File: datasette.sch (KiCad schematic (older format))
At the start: 40 parts, among them CN15 CONN_IEC_INT, CN16 CONN_TAPE_INT, CN3 CASSETTE, CN7 SERIAL_BUS, CN93 C64_STYLE_CASSETTE, Q5 2SD880, U9 74LS06, U91 DT1042, U92 DT1042

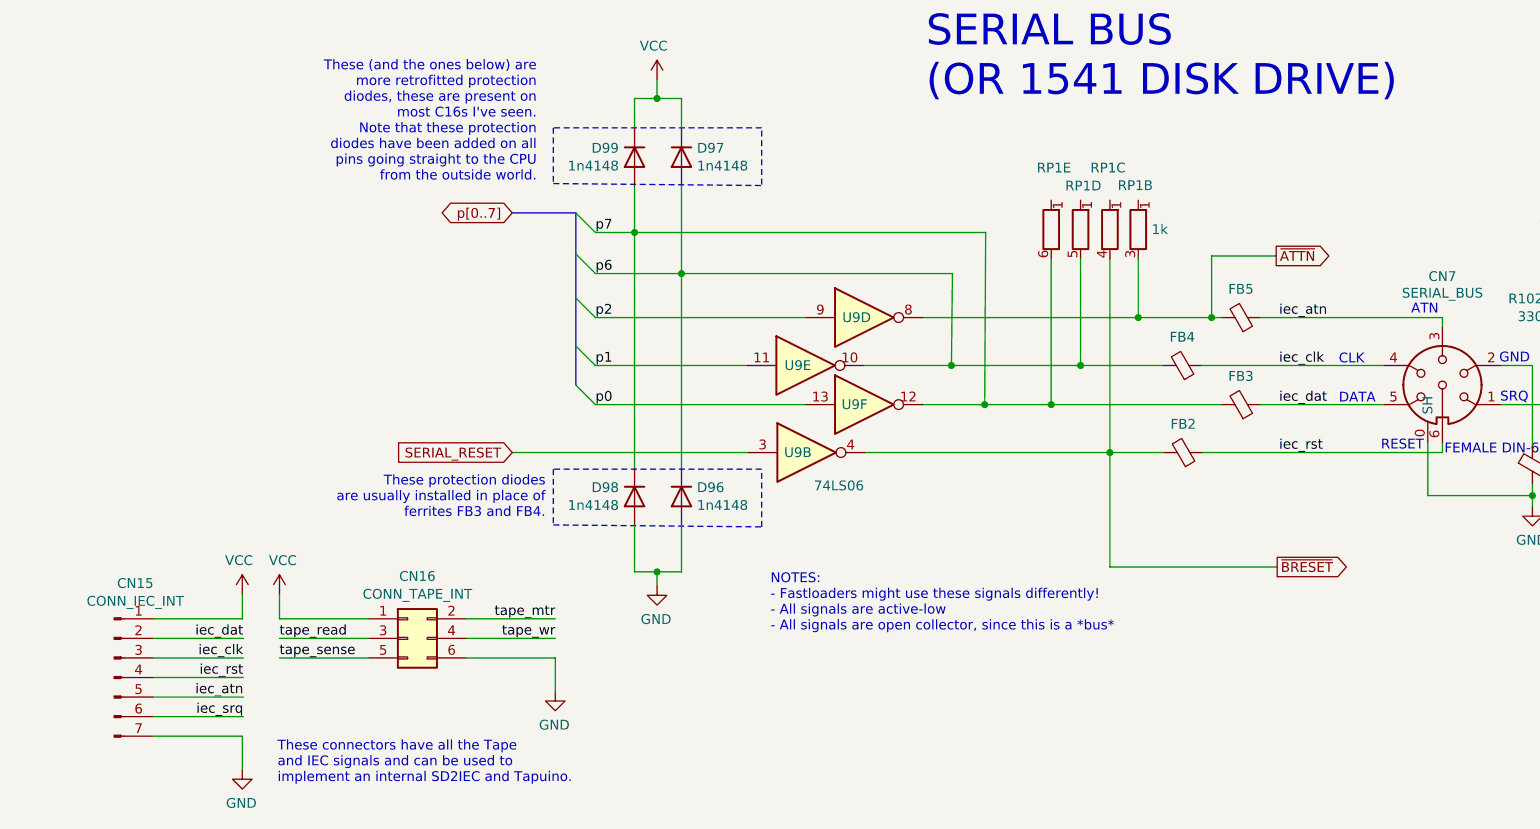
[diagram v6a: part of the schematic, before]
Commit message: Add jumper to select which reset signal is brought to IEC connector
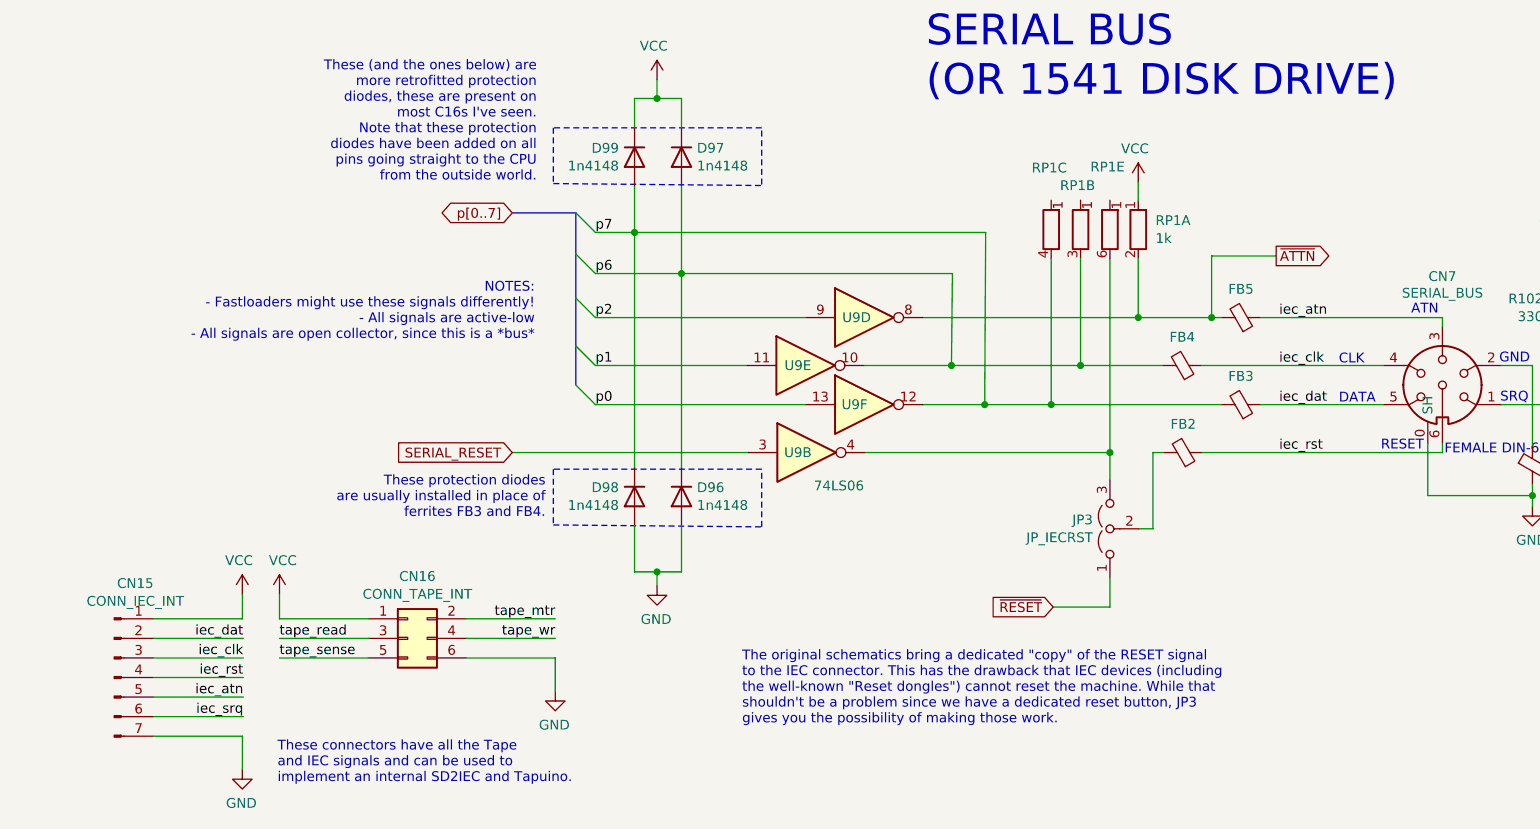
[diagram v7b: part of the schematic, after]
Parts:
- removed unit 4 of RP1
- added JP3: JP_IECRST, Jumper:SolderJumper-3_P1.3mm_Open_RoundedPad1.0x1.5mm, symbol Jumper:Jumper_3_Open
- added unit 1 of RP1
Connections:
- net VCC: now also RP1.1 (R1.1)
- net p6: now also RP1.3 (R2.2)
- net p7: now also RP1.4 (R3.2); no longer RP1.6 (R5.2)
- net ~ATTN: now also RP1.2 (R1.2); no longer RP1.3 (R2.2)
- removed net ~BRESET: FB2.2, RP1.4 (R3.2), U9.4
- new net: JP3.3 (B), RP1.6 (R5.2), U9.4
- new net: FB2.2, JP3.2 (C)
- new net ~RESET: JP3.1 (A)
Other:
- note added: "The original schematics bring a dedicated "copy" of the RESET signal\nto the IEC connector. This has the drawback that IEC devices (including\nthe well-known "Reset dongles") cannot reset the machine. While that\nshouldn't be a problem since we have a dedicated reset button, JP3 \ngives you the possibility of making those work."
- moved on the sheet: RP1B, RP1C, RP1E
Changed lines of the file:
@@
 Sheet 7 14
 Title "LittleSixteen"
-Date "2024-08-07"
+Date "2024-08-11"
 Rev "4git"
 Comp "SukkoPera"
@@
 Wire Wire Line
 	7505 5865 6280 5865
-Wire Wire Line
-	6080 5865 5805 5865
 $Comp
 L 74xx:74LS06 U9
@@
 Wire Wire Line
 	5805 4875 5805 5865
-Connection ~ 5805 5865
 Wire Wire Line
 	5805 5865 4555 5865
@@
 Text Notes 7795 5415 0    50   ~ 0
 GND
-Text Notes 4070 6785 0    50   ~ 0
-NOTES:\n- Fastloaders might use these signals differently!\n- All signals are active-low\n- All signals are open collector, since this is a *bus*
 Connection ~ 3010 2425
 Wire Notes Line
@@
 ~ATTN
 Wire Wire Line
-	5805 5865 5805 6450
-Wire Wire Line
-	5805 6450 6660 6450
-Text GLabel 6660 6450 2    50   Output ~ 0
-~BRESET
-Wire Wire Line
 	5880 1535 6100 1535
 Text Notes 6895 1770 0    50   ~ 0
@@
 $Comp
 L Device:R_Network05_Split RP1
-U 5 1 64605429
+U 3 1 646039C4
 P 5505 4725
-F 0 "RP1" H 5519 5040 50  0000 C CNN
-F 1 "1k" H 6060 4725 50  0000 C CNN
+F 0 "RP1" H 5405 5040 50  0000 L CNN
+F 1 "1k" H 5603 4672 50  0001 L CNN
 F 2 "Resistor_THT:R_Array_SIP6" V 5425 4725 50  0001 C CNN
 F 3 "http://www.vishay.com/docs/31509/csc.pdf" H 5505 4725 50  0001 C CNN
 F 4 "Bussed" H 5505 4725 50  0001 C CNN "Notes"
-	5    5505 4725
+	3    5505 4725
 	1    0    0    -1
 $EndComp
 $Comp
 L Device:R_Network05_Split RP1
-U 4 1 646047D0
+U 2 1 64602B24
 P 5655 4725
-F 0 "RP1" H 5669 4948 50  0000 C CNN
+F 0 "RP1" H 5550 4950 50  0000 L CNN
 F 1 "1k" H 5753 4672 50  0001 L CNN
 F 2 "Resistor_THT:R_Array_SIP6" V 5575 4725 50  0001 C CNN
 F 3 "http://www.vishay.com/docs/31509/csc.pdf" H 5655 4725 50  0001 C CNN
 F 4 "Bussed" H 5655 4725 50  0001 C CNN "Notes"
-	4    5655 4725
-	1    0    0    -1
-$EndComp
-$Comp
-L Device:R_Network05_Split RP1
-U 3 1 646039C4
-P 5805 4725
-F 0 "RP1" H 5705 5040 50  0000 L CNN
-F 1 "1k" H 5903 4672 50  0001 L CNN
-F 2 "Resistor_THT:R_Array_SIP6" V 5725 4725 50  0001 C CNN
-F 3 "http://www.vishay.com/docs/31509/csc.pdf" H 5805 4725 50  0001 C CNN
-F 4 "Bussed" H 5805 4725 50  0001 C CNN "Notes"
-	3    5805 4725
-	1    0    0    -1
-$EndComp
-$Comp
-L Device:R_Network05_Split RP1
-U 2 1 64602B24
-P 5950 4725
-F 0 "RP1" H 5845 4950 50  0000 L CNN
-F 1 "1k" H 6048 4672 50  0001 L CNN
-F 2 "Resistor_THT:R_Array_SIP6" V 5870 4725 50  0001 C CNN
-F 3 "http://www.vishay.com/docs/31509/csc.pdf" H 5950 4725 50  0001 C CNN
-F 4 "Bussed" H 5950 4725 50  0001 C CNN "Notes"
-	2    5950 4725
+	2    5655 4725
 	1    0    0    -1
 $EndComp
@@
 $EndComp
 $Comp
+L emi_filter_3pin:EMI_Filter_3Pin FB3
+U 1 1 670A70CA
+P 6475 5620
+F 0 "FB3" V 6620 5620 50  0000 C CNN
+F 1 "DSS1NB32A271Q91A" H 6575 5575 50  0001 L CNN
+F 2 "LittleSixteen:EMI_Filter" V 6405 5620 50  0001 C CNN
+F 3 "~" H 6475 5620 50  0001 C CNN
+	1    6475 5620
+	0    1    -1   0
+$EndComp
+$Comp
+L emi_filter_3pin:EMI_Filter_3Pin FB4
+U 1 1 670A7799
+P 6175 5420
+F 0 "FB4" V 6320 5420 50  0000 C CNN
+F 1 "DSS1NB32A271Q91A" H 6275 5375 50  0001 L CNN
+F 2 "LittleSixteen:EMI_Filter" V 6105 5420 50  0001 C CNN
+F 3 "~" H 6175 5420 50  0001 C CNN
+	1    6175 5420
+	0    1    -1   0
+$EndComp
+$Comp
+L emi_filter_3pin:EMI_Filter_3Pin FB5
+U 1 1 670A7ED0
+P 6475 5175
+F 0 "FB5" V 6620 5175 50  0000 C CNN
+F 1 "DSS1NB32A271Q91A" H 6575 5130 50  0001 L CNN
+F 2 "LittleSixteen:EMI_Filter" V 6405 5175 50  0001 C CNN
+F 3 "~" H 6475 5175 50  0001 C CNN
+	1    6475 5175
+	0    1    -1   0
+$EndComp
+$Comp
+L emi_filter_3pin:EMI_Filter_3Pin FB1
+U 1 1 670A8919
+P 7965 5930
+F 0 "FB1" H 8065 5930 50  0000 L CNN
+F 1 "DSS1NB32A271Q91A" H 8065 5885 50  0001 L CNN
+F 2 "LittleSixteen:EMI_Filter" V 7895 5930 50  0001 C CNN
+F 3 "~" H 7965 5930 50  0001 C CNN
+	1    7965 5930
+	1    0    0    -1
+$EndComp
+Wire Wire Line
+	7430 6085 7965 6085
+$Comp
+L Jumper:Jumper_3_Open JP12
+U 1 1 66B76798
+P 6250 1535
+F 0 "JP12" V 6204 1621 50  0000 L CNN
+F 1 "JMP_TPSENSE" V 6295 1621 50  0000 L CNN
+F 2 "Connector_PinHeader_2.54mm:PinHeader_1x03_P2.54mm_Vertical" H 6250 1535 50  0001 C CNN
+F 3 "~" H 6250 1535 50  0001 C CNN
+	1    6250 1535
+	0    1    1    0
+$EndComp
+Wire Wire Line
+	6250 1285 6250 1110
+Wire Wire Line
+	6250 1110 6440 1110
+Wire Wire Line
+	6250 1785 6250 1960
+Text Notes 6070 995  0    50   ~ 0
+JP12 replicates JP8/9 of the Plus/4\nSet to 1-2 unless you know what you are doing
+Text Label 6650 2325 0    50   ~ 0
+p6
+Text GLabel 6980 2225 2    50   Input ~ 0
+p[0..7]
+Wire Wire Line
+	6575 2325 6810 2325
+Text Label 6515 1960 0    50   ~ 0
+p7
+Text GLabel 6895 1860 2    50   Output ~ 0
+p[0..7]
+Wire Wire Line
+	6250 1960 6675 1960
+Entry Wire Line
+	6810 2325 6910 2225
+Wire Bus Line
+	6910 2225 6980 2225
+Entry Wire Line
+	6675 1960 6775 1860
+Wire Bus Line
+	6775 1860 6895 1860
+$Comp
 L emi_filter_3pin:EMI_Filter_3Pin FB2
 U 1 1 6707F003
@@
 	0    1    -1   0
 $EndComp
-$Comp
-L emi_filter_3pin:EMI_Filter_3Pin FB3
-U 1 1 670A70CA
-P 6475 5620
-F 0 "FB3" V 6620 5620 50  0000 C CNN
-F 1 "DSS1NB32A271Q91A" H 6575 5575 50  0001 L CNN
-F 2 "LittleSixteen:EMI_Filter" V 6405 5620 50  0001 C CNN
-F 3 "~" H 6475 5620 50  0001 C CNN
-	1    6475 5620
-	0    1    -1   0
-$EndComp
-$Comp
-L emi_filter_3pin:EMI_Filter_3Pin FB4
-U 1 1 670A7799
-P 6175 5420
-F 0 "FB4" V 6320 5420 50  0000 C CNN
-F 1 "DSS1NB32A271Q91A" H 6275 5375 50  0001 L CNN
-F 2 "LittleSixteen:EMI_Filter" V 6105 5420 50  0001 C CNN
-F 3 "~" H 6175 5420 50  0001 C CNN
-	1    6175 5420
-	0    1    -1   0
-$EndComp
-$Comp
-L emi_filter_3pin:EMI_Filter_3Pin FB5
-U 1 1 670A7ED0
-P 6475 5175
-F 0 "FB5" V 6620 5175 50  0000 C CNN
-F 1 "DSS1NB32A271Q91A" H 6575 5130 50  0001 L CNN
-F 2 "LittleSixteen:EMI_Filter" V 6405 5175 50  0001 C CNN
-F 3 "~" H 6475 5175 50  0001 C CNN
-	1    6475 5175
-	0    1    -1   0
-$EndComp
-$Comp
-L emi_filter_3pin:EMI_Filter_3Pin FB1
-U 1 1 670A8919
-P 7965 5930
-F 0 "FB1" H 8065 5930 50  0000 L CNN
-F 1 "DSS1NB32A271Q91A" H 8065 5885 50  0001 L CNN
-F 2 "LittleSixteen:EMI_Filter" V 7895 5930 50  0001 C CNN
-F 3 "~" H 7965 5930 50  0001 C CNN
-	1    7965 5930
-	1    0    0    -1
-$EndComp
-Wire Wire Line
-	7430 6085 7965 6085
-$Comp
-L Jumper:Jumper_3_Open JP12
-U 1 1 66B76798
-P 6250 1535
-F 0 "JP12" V 6204 1621 50  0000 L CNN
-F 1 "JMP_TPSENSE" V 6295 1621 50  0000 L CNN
-F 2 "Connector_PinHeader_2.54mm:PinHeader_1x03_P2.54mm_Vertical" H 6250 1535 50  0001 C CNN
-F 3 "~" H 6250 1535 50  0001 C CNN
-	1    6250 1535
-	0    1    1    0
-$EndComp
-Wire Wire Line
-	6250 1285 6250 1110
-Wire Wire Line
-	6250 1110 6440 1110
-Wire Wire Line
-	6250 1785 6250 1960
-Text Notes 6070 995  0    50   ~ 0
-JP12 replicates JP8/9 of the Plus/4\nSet to 1-2 unless you know what you are doing
-Text Label 6650 2325 0    50   ~ 0
-p6
-Text GLabel 6980 2225 2    50   Input ~ 0
-p[0..7]
-Wire Wire Line
-	6575 2325 6810 2325
-Text Label 6515 1960 0    50   ~ 0
-p7
-Text GLabel 6895 1860 2    50   Output ~ 0
-p[0..7]
-Wire Wire Line
-	6250 1960 6675 1960
-Entry Wire Line
-	6810 2325 6910 2225
-Wire Bus Line
-	6910 2225 6980 2225
-Entry Wire Line
-	6675 1960 6775 1860
-Wire Bus Line
-	6775 1860 6895 1860
+Text Notes 2865 5295 2    50   ~ 0
+NOTES:\n- Fastloaders might use these signals differently!\n- All signals are active-low\n- All signals are open collector, since this is a *bus*
+Text GLabel 5515 6655 0    50   Input ~ 0
+~RESET
+$Comp
+L Jumper:Jumper_3_Open JP3
+U 1 1 66BD1BAC
+P 5805 6255
+F 0 "JP3" V 5851 6342 50  0000 L CNN
+F 1 "JP_IECRST" V 5760 6342 50  0000 L CNN
+F 2 "Jumper:SolderJumper-3_P1.3mm_Open_RoundedPad1.0x1.5mm" H 5805 6255 50  0001 C CNN
+F 3 "~" H 5805 6255 50  0001 C CNN
+	1    5805 6255
+	0    -1   -1   0
+$EndComp
+Wire Wire Line
+	5805 6005 5805 5865
+Connection ~ 5805 5865
+Wire Wire Line
+	5955 6255 6025 6255
+Wire Wire Line
+	6025 6255 6025 5865
+Wire Wire Line
+	6025 5865 6080 5865
+Wire Wire Line
+	5805 6505 5805 6655
+Wire Wire Line
+	5805 6655 5515 6655
+Text Notes 3925 7260 0    50   ~ 0
+The original schematics bring a dedicated "copy" of the RESET signal\nto the IEC connector. This has the drawback that IEC devices (including\nthe well-known "Reset dongles") cannot reset the machine. While that\nshouldn't be a problem since we have a dedicated reset button, JP3 \ngives you the possibility of making those work.
+$Comp
+L Device:R_Network05_Split RP1
+U 1 1 66C2C54E
+P 5950 4725
+AR Path="/5ECB474B/66C2C54E" Ref="RP1"  Part="1"
+AR Path="/5EACE220/66C2C54E" Ref="RP?"  Part="1"
+F 0 "RP1" H 6038 4771 50  0000 L CNN
+F 1 "1k" H 6038 4680 50  0000 L CNN
+F 2 "Resistor_THT:R_Array_SIP6" V 5870 4725 50  0001 C CNN
+F 3 "http://www.vishay.com/docs/31509/csc.pdf" H 5950 4725 50  0001 C CNN
+F 4 "Bussed" H 5950 4725 50  0001 C CNN "Notes"
+	1    5950 4725
+	1    0    0    -1
+$EndComp
+$Comp
+L Device:R_Network05_Split RP1
+U 5 1 64605429
+P 5805 4725
+F 0 "RP1" H 5705 5045 50  0000 L CNN
+F 1 "1k" H 6360 4725 50  0001 C CNN
+F 2 "Resistor_THT:R_Array_SIP6" V 5725 4725 50  0001 C CNN
+F 3 "http://www.vishay.com/docs/31509/csc.pdf" H 5805 4725 50  0001 C CNN
+F 4 "Bussed" H 5805 4725 50  0001 C CNN "Notes"
+	5    5805 4725
+	1    0    0    -1
+$EndComp
+Wire Wire Line
+	5950 4485 5950 4575
+$Comp
+L power:VCC #PWR?
+U 1 1 66C66638
+P 5950 4485
+AR Path="/5E4A81E1/66C66638" Ref="#PWR?"  Part="1"
+AR Path="/5EACE220/66C66638" Ref="#PWR?"  Part="1"
+F 0 "#PWR?" H 5950 4335 50  0001 C CNN
+F 1 "VCC" H 5967 4658 50  0000 C CNN
+F 2 "" H 5950 4485 50  0001 C CNN
+F 3 "" H 5950 4485 50  0001 C CNN
+	1    5950 4485
+	-1   0    0    -1
+$EndComp
 Wire Bus Line
 	3075 4640 3075 5520
